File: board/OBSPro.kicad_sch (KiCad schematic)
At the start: 4 parts

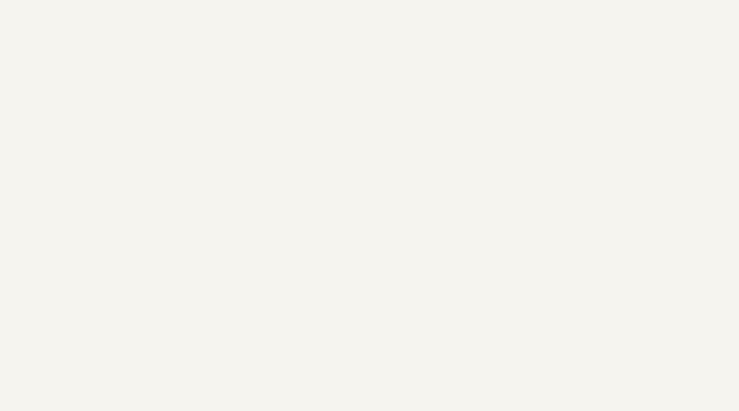
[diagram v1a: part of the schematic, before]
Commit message: 3D-Modelle hinzugefügt
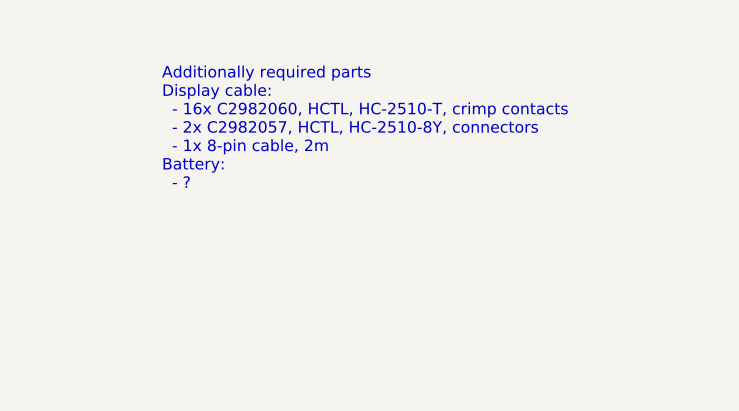
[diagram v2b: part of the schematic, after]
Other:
- note added: "Additionally required parts Display cable: - 16x C2982060, HCTL, HC-2510-T, crimp contacts - 2x C2982057, HCTL, HC-2510-8Y, connectors - 1x 8-pin cable, 2m Battery: - ?"
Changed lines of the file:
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@@
 (kicad_sch (version 20230121) (generator eeschema)
   (paper "A4")
+  (text "Additionally required parts\nDisplay cable:\n  - 16x C2982060, HCTL, HC-2510-T, crimp contacts\n  - 2x C2982057, HCTL, HC-2510-8Y, connectors\n  - 1x 8-pin cable, 2m\nBattery:\n  - ?\n"
+    (at 181.61 53.34 0)
+    (effects (font (size 1.27 1.27)) (justify left bottom))
+  )
   (symbol (lib_id "Mechanical:MountingHole") (at 54.61 58.42 0) (unit 1)
     (in_bom yes) (on_board yes) (dnp no) (fields_autoplaced)

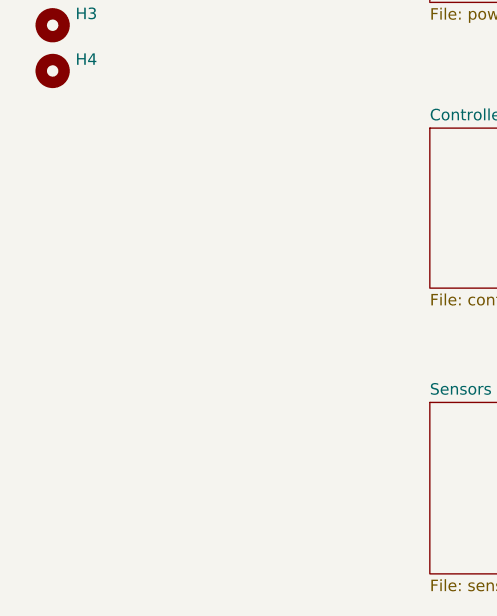
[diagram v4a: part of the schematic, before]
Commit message: Update schematic and PCB layout
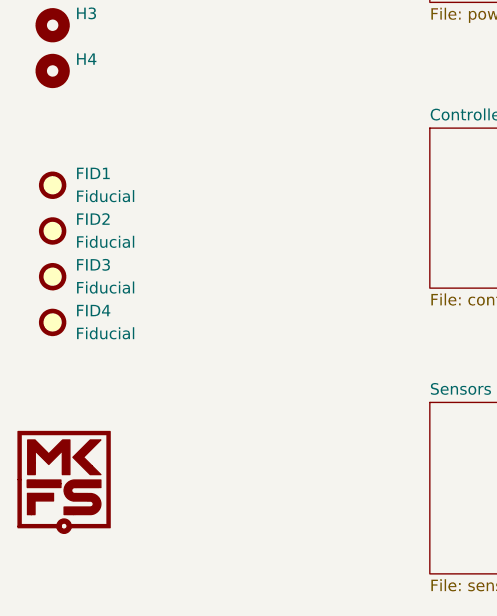
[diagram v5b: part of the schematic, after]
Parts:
- added FID1, FID2, FID3, FID4: Fiducial, Fiducial:Fiducial_0.5mm_Mask1.5mm, symbol Mechanical:Fiducial
- added G1: MKFS_Logo, OBSPro:Logo_MKFS, symbol MKFS:MKFS_Logo

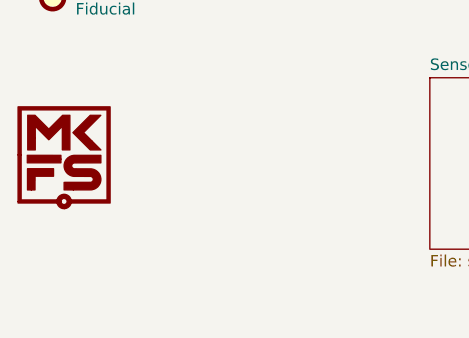
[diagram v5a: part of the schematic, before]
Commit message: Add OBS Logo, fix charge IC 3D model, update errata
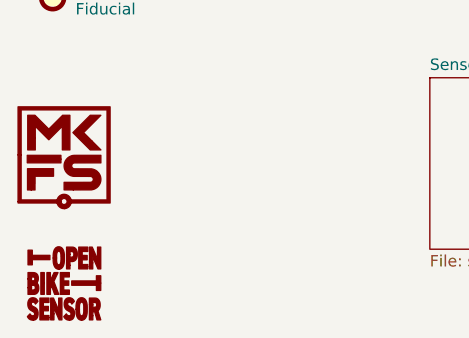
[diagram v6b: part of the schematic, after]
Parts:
- added G2: OBS_Logo, OBSPro:OBS_Logo, symbol OBSPro:OBS_Logo
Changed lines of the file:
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@@
+	)
+	(symbol
+		(lib_id "OBSPro:OBS_Logo")
+		(at 55.88 123.19 0)
+		(unit 1)
+		(exclude_from_sim no)
+		(in_bom yes)
+		(on_board yes)
+		(dnp no)
+		(fields_autoplaced yes)
+		(property "Reference" "G2"
+			(at 55.88 118.745 0)
+			(effects
+				(font
+					(size 1.27 1.27)
+				)
+				(hide yes)
+			)
+		)
+		(property "Value" "OBS_Logo"
+			(at 55.88 127.635 0)
+			(effects
+				(font
+					(size 1.27 1.27)
+				)
+				(hide yes)
+			)
+		)
+		(property "Footprint" "OBSPro:OBS_Logo"
+			(at 55.88 123.19 0)
+			(effects
+				(font
+					(size 1.27 1.27)
+				)
+				(hide yes)
+			)
+		)
+		(property "Datasheet" ""
+			(at 55.88 123.19 0)
+			(effects
+				(font
+					(size 1.27 1.27)
+				)
+				(hide yes)
+			)
+		)
+		(property "Description" ""
+			(at 55.88 123.19 0)
+			(effects
+				(font
+					(size 1.27 1.27)
+				)
+				(hide yes)
+			)
+		)
+		(property "MPN" ""
+			(at 55.88 123.19 0)
+			(effects
+				(font
+					(size 1.27 1.27)
+				)
+				(hide yes)
+			)
+		)
+		(property "Manufacturer" ""
+			(at 55.88 123.19 0)
+			(effects
+				(font
+					(size 1.27 1.27)
+				)
+				(hide yes)
+			)
+		)
+		(instances
+			(project ""
+				(path "/1b575199-a76e-4620-8a1a-43f78ed7da24"
+					(reference "G2")
+					(unit 1)
+				)
+			)
+		)
 	)
 	(symbol
